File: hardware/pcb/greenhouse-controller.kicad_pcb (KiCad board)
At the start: 2 copper layers, 208 x 132 mm, 68 parts, among them J1 Motor 2, J10 ALARM contact, J11 AC-Mains, J12 DM1AA-SF-PEJ72, J2 24V in, J3 I2C Display, J4 Keypad, J5 MODBUS RS485 S200, J6 Motor 3, J7 Motor 1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

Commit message: Some corrections
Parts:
- added M1: LCD1602 I2C Module mechanical, my-KiCad-library:LCD1602 I2C Module mechanical, F.Cu at (-47.0, 0.00)
- moved P1 2.25 mm to (76.2, 34.0)
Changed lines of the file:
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@@
 		)
 	)
+	(footprint "my-KiCad-library:LCD1602 I2C Module mechanical"
+		(layer "F.Cu")
+		(at -47 0)
+		(property "Reference" "M1"
+			(at 0 -0.5 0)
+			(unlocked yes)
+			(layer "F.SilkS")
+			(effects
+				(font
+					(size 1 1)
+					(thickness 0.1)
+				)
+			)
+		)
+		(property "Value" "LCD1602 I2C Module mechanical"
+			(at 0 1 0)
+			(unlocked yes)
+			(layer "F.Fab")
+			(effects
+				(font
+					(size 1 1)
+					(thickness 0.15)
+				)
+			)
+		)
+		(property "Datasheet" ""
+			(at 0 0 0)
+			(unlocked yes)
+			(layer "F.Fab")
+			(hide yes)
+			(effects
+				(font
+					(size 1 1)
+					(thickness 0.15)
+				)
+			)
+		)
+		(property "Description" ""
+			(at 0 0 0)
+			(unlocked yes)
+			(layer "F.Fab")
+			(hide yes)
+			(effects
+				(font
+					(size 1 1)
+					(thickness 0.15)
+				)
+			)
+		)
+		(sheetname "/")
+		(sheetfile "greenhouse-controller.kicad_sch")
+		(attr through_hole)
+		(fp_rect
+			(start -43.5 -16)
+			(end 43.5 16)
+			(stroke
+				(width 0.1)
+				(type dash)
+			)
+			(fill no)
+			(layer "F.SilkS")
+		)
+		(fp_rect
+			(start -43.5 -7)
+			(end -38 7)
+			(stroke
+				(width 0.1)
+				(type dot)
+			)
+			(fill no)
+			(layer "F.SilkS")
+		)
+		(fp_rect
+			(start -35.65 -13.4)
+			(end 35.65 13.4)
+			(stroke
+				(width 0.05)
+				(type solid)
+			)
+			(fill no)
+			(layer "F.Fab")
+		)
+		(fp_rect
+			(start -32.25 -8)
+			(end 32.25 8)
+			(stroke
+				(width 0.05)
+				(type solid)
+			)
+			(fill no)
+			(layer "F.Fab")
+		)
+		(fp_text user "LCD1602 I2C Module mechanical"
+			(at -20 15 0)
+			(unlocked yes)
+			(layer "F.SilkS")
+			(effects
+				(font
+					(size 1.27 1.27)
+					(thickness 0.15)
+				)
+			)
+		)
+		(fp_text user "${REFERENCE}"
+			(at 0 2.5 0)
+			(unlocked yes)
+			(layer "F.Fab")
+			(effects
+				(font
+					(size 1 1)
+					(thickness 0.15)
+				)
+			)
+		)
+		(pad "" np_thru_hole circle
+			(at -40 -12.5)
+			(size 7 7)
+			(drill 3.2)
+			(layers "*.Cu" "*.Mask")
+		)
+		(pad "" np_thru_hole circle
+			(at -40 12.5)
+			(size 7 7)
+			(drill 3.2)
+			(layers "*.Cu" "*.Mask")
+		)
+		(pad "" np_thru_hole circle
+			(at 40 -12.5)
+			(size 7 7)
+			(drill 3.2)
+			(layers "*.Cu" "*.Mask")
+		)
+		(pad "" np_thru_hole circle
+			(at 40 12.5)
+			(size 7 7)
+			(drill 3.2)
+			(layers "*.Cu" "*.Mask")
+		)
+		(embedded_fonts no)
+	)
 	(footprint "Resistor_SMD:R_1206_3216Metric_Pad1.30x1.75mm_HandSolder"
 		(layer "F.Cu")
@@
 	(footprint "my-KiCad-library:Meanwell RS-15 Mechanical"
 		(layer "F.Cu")
-		(at 77.274 32 90)
+		(at 76.25 34 90)
 		(property "Reference" "P1"
 			(at 31.25 -1.5 90)

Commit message: ìntermediate update of PCB design
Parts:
- moved D14 120.8 mm to (0.00, 32.0)
- moved R22 118.6 mm to (0.00, 36.0), turned to 0 degrees
- moved R24 81.1 mm to (-86.5, 36.0), turned to 0 degrees
- moved D15 77.4 mm to (-89.1, 32.0)
- moved R5 59.3 mm to (-51.5, -27.0), turned to 180 degrees
- moved R16 59.2 mm to (-75.0, -27.0), turned to 180 degrees
- moved R10 59.2 mm to (-28.3, -27.0), turned to 180 degrees
- moved R3 59.1 mm to (-53.1, 28.0), turned to 0 degrees
- moved R14 57.1 mm to (-75.7, 27.0), turned to 0 degrees
- moved R8 57.1 mm to (-30.7, 27.0), turned to 0 degrees
- moved Q5 47.5 mm to (-74.5, 22.0), turned to 180 degrees
- moved Q1 47.4 mm to (-52.0, 22.0), turned to 180 degrees
- moved Q3 47.3 mm to (-29.5, 22.0), turned to 180 degrees
- moved Q2 47.1 mm to (-52.7, -21.0), turned to 0 degrees
- moved Q6 47.1 mm to (-76.3, -21.0), turned to 0 degrees
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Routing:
- net /24V: track 0.00 -> 125.5 mm
- net /24V_GND: track 0.00 -> 112.7 mm
- net /GND: track 0.00 -> 107.8 mm, vias 0 -> 2
- net /SD_CS: track 0.00 -> 101.3 mm
- net Net-(BT1-+): track 0.00 -> 99.2 mm, vias 0 -> 1
- net /SD_MOSI: track 0.00 -> 97.9 mm
- net Net-(J11-Pin_1): track 0.00 -> 93.1 mm
- net Net-(J11-Pin_2): track 0.00 -> 92.1 mm
- net /SD_CLK: track 0.00 -> 91.9 mm
- net Net-(J11-Pin_3): track 0.00 -> 88.3 mm
- net /SD_MISO: track 0.00 -> 85.8 mm
- net /KP_COL1: track 0.00 -> 77.4 mm
- net /KP_ROW4: track 0.00 -> 75.4 mm
- net /KP_ROW3: track 0.00 -> 73.3 mm
- net /KP_ROW2: track 0.00 -> 71.1 mm
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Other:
- board text added: "HB"
- board text added: "PWR"

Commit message: Intermediate update PCB
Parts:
- moved U3 8.28 mm to (6.35, 10.2)
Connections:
- J2 pad 1: /24V_GND -> /GND
- J5 pad 2: /24V_GND -> /GND
- P1 pad 4: /24V_GND -> /GND
- U2 pad 1: Net-(F1-Pad2) -> /24V
- U2 pad 2: Net-(F1-Pad2) -> /24V
- U2 pad 3: /24V_GND -> /GND
- U2 pad 4: /24V_GND -> /GND
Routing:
- net /GND: track 107.8 -> 315.4 mm
- net /HB_LED: track 0.00 -> 153.2 mm, vias 0 -> 1
- net /24V_GND: track 112.7 -> 0.00 mm
- net /24V: track 125.5 -> 221.5 mm
- net /RS485-B: track 12.6 -> 55.4 mm
- net /RS485-A: track 12.5 -> 29.4 mm
- net Net-(F1-Pad2): track 2.54 -> 0.00 mm
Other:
- board text added: "24V"
- board text added: "A"
- board text added: "B"
- board text added: "GND"
- board text added: "RS485"

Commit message: intermediate update PCB
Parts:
- added J8: Load enable, Connector_PinHeader_2.54mm:PinHeader_1x02_P2.54mm_Vertical, F.Cu at (15.0, 26.7)
- moved R21 3.68 mm to (7.34, 26.7)
- moved R3 1.35 mm to (-53.3, 26.7)
- moved R14 0.33 mm to (-75.7, 26.7)
- moved R8 0.33 mm to (-30.7, 26.7)
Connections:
- R21 pad 2: /RS485-B -> Net-(J8-Pin_2)
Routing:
- net /RS485_DI: track 0.00 -> 60.8 mm
- net Net-(J6-Pin_3): track 0.00 -> 58.3 mm
- net Net-(J1-Pin_3): track 0.00 -> 57.6 mm
- net Net-(J7-Pin_3): track 0.00 -> 56.9 mm
- net /RS485_DE_RE: track 0.00 -> 54.1 mm
- net Net-(J6-Pin_4): track 0.00 -> 52.2 mm
- net Net-(J1-Pin_4): track 0.00 -> 51.7 mm
- net Net-(J7-Pin_4): track 0.00 -> 51.2 mm
- net Net-(J1-Pin_2): track 0.00 -> 49.9 mm
- net Net-(J6-Pin_2): track 0.00 -> 49.8 mm
- net Net-(J7-Pin_2): track 0.00 -> 49.2 mm
- net /RS485_RO: track 0.00 -> 48.9 mm
- net Net-(J7-Pin_1): track 0.00 -> 39.8 mm
- net Net-(J1-Pin_1): track 0.00 -> 39.3 mm
- net Net-(J6-Pin_1): track 0.00 -> 38.9 mm
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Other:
- board text added: "CLOSE"
- board text added: "OPEN"

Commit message: First alpha release of PCB
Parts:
- added G***: LOGO_LogoRFSee_28x5-6mm, my-KiCad-library:LOGO_LogoRFSee_28x5-6mm, F.Cu at (181.6, 104.1)
- added G***: LOGO_LogoRFSee_37x8mm, my-KiCad-library:LOGO_LogoRFSee_37x8mm, F.Cu at (83.8, 47.0)
- moved Q3 173.6 mm to (118.5, 112.8)
- moved Q1 173.6 mm to (96.0, 112.8)
- moved Q5 173.6 mm to (73.5, 112.8)
- moved R14 173.6 mm to (72.2, 117.5)
- moved R3 173.6 mm to (94.6, 117.5)
- moved R8 173.6 mm to (117.2, 117.5)
- moved R5 173.5 mm to (96.5, 63.5)
- moved R10 173.4 mm to (119.7, 63.5)
- moved R16 173.4 mm to (73.0, 63.5)
- moved BT1 173.3 mm to (135.0, 31.1)
- moved C2 173.3 mm to (184.2, 54.6)
- moved D10 173.3 mm to (84.0, 122.2)
- moved D13 173.3 mm to (158.1, 125.1)
- moved D14 173.3 mm to (148.0, 122.2)
- moved D15 173.3 mm to (58.9, 122.2)
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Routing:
- net /GND: track 348.2 -> 696.1 mm, vias 5 -> 247
- net /5V: track 68.0 -> 364.8 mm, vias 0 -> 6
- net /OPTO_INPUT: track 8.87 -> 247.2 mm
- net /3V3: track 69.6 -> 190.8 mm, vias 1 -> 4
- net /RELAY_M1_CLOSE: track 0.00 -> 120.2 mm, vias 0 -> 1
- net /RELAY_M1_OPEN: track 0.00 -> 116.9 mm, vias 0 -> 1
- net /RELAY_M2_OPEN: track 5.34 -> 115.0 mm, vias 0 -> 2
- net /RELAY_M3_OPEN: track 5.31 -> 93.3 mm, vias 0 -> 1
- net /RELAY_M3_CLOSE: track 0.00 -> 77.7 mm
- net /RELAY_M2_CLOSE: track 0.00 -> 72.1 mm
- net Net-(D10-K): track 5.90 -> 70.0 mm, vias 0 -> 1
- net Net-(D3-K): track 5.90 -> 69.8 mm, vias 0 -> 1
- net Net-(D6-K): track 5.90 -> 68.9 mm, vias 0 -> 1
- net Net-(D11-A): track 25.2 -> 37.8 mm
- net /SD_MOSI: track 97.9 -> 86.2 mm
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- added copper zone on B.Cu, net /GND
- added copper zone on F.Cu, net /GND
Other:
- outline, holes or cut-outs redrawn
- board text added: "+24V"
- board text added: "220V AC"
- board text added: "ALARM IN"
- board text added: "DICHT"
- board text added: "E"
- board text added: "Enable Load"
- board text added: "K1"
- board text added: "K2"
- board text added: "K3"
- board text added: "K4"
- board text added: "KAS-Controller"
- board text added: "Keypad"
- board text added: "L"
- board text added: "LCD Display"
- board text added: "M1"
- board text added: "M2"
- board text added: "M3"
- board text added: "Motor 1"
- board text added: "Motor 2"
- board text added: "Motor 3"
- board text added: "N"
- board text added: "R1"
- board text added: "R2"
- board text added: "R3"
- board text added: "R4"
- board text added: "RS485 / S200"
- board text added: "RTC Backup"
- board text added: "RUN"
- board text added: "Remko Welling (remko@rfsee.nl) 14-4-2026"
- board text added: "SCL"
- board text added: "SD-Card"
- board text added: "SDA"
- board text added: "VCC"
- board text removed: "HB"

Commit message: Solved final error in PCB, outline Fab text corrected
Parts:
- D14: value LED Amber -> Amber
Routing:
- net /5V: track 364.8 -> 390.6 mm, vias 6 -> 7
- net /GND: vias 247 -> 249
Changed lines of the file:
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@@
 		)
 		(property "Value" "SM712_SOT23"
-			(at 0 2.4 90)
+			(at 4.191 -0.127 180)
 			(layer "F.Fab")
 			(effects
@@
 			)
 		)
-		(property "Value" "LED Amber"
+		(property "Value" "Amber"
 			(at 0 1.65 0)
 			(layer "F.Fab")
@@
 		(tags "capacitor handsolder")
 		(property "Reference" "C3"
-			(at 0 -1.85 0)
+			(at 3.683 0 0)
 			(layer "F.SilkS")
 			(effects
@@
 		)
 		(property "Value" "BUCK-30V-5V"
-			(at 0.0508 -0.127 90)
+			(at 0.0508 -0.127 180)
 			(layer "F.Fab")
 			(effects
@@
 		)
 		(property "Value" "Battery_Cell"
-			(at 12.4 13 270)
+			(at 15.875 -0.173 0)
 			(unlocked yes)
 			(layer "F.Fab")
@@
 		)
 		(fp_text user "${REFERENCE}"
-			(at 12.4 0 270)
+			(at 12.4 0 0)
 			(unlocked yes)
 			(layer "F.Fab")
@@
 		(descr "DS26, Crystal, length 6.0mm, width 2.0mm, THT, https://www.microcrystal.com/fileadmin/Media/Products/32kHz/Datasheet/DS-Series.pdf")
 		(property "Reference" "Y1"
-			(at -1.74 1.625 90)
+			(at 4.043 3.175 180)
 			(layer "F.SilkS")
 			(effects
@@
 		)
 		(property "Value" "32.768 kHz"
-			(at 3.64 1.625 90)
+			(at 0.995 12.065 180)
 			(layer "F.Fab")
 			(effects
@@
 		)
 		(fp_text user "${REFERENCE}"
-			(at 0.95 4.95 90)
+			(at 0.95 10.287 180)
 			(layer "F.Fab")
 			(effects
@@
 		)
 		(property "Value" "I2C Display"
-			(at 0 10 90)
+			(at -0.127 14.097 180)
 			(layer "F.Fab")
 			(effects
@@
 		)
 		(property "Value" "Load enable"
-			(at 0 4.92 90)
+			(at -2.54 4.419 180)
 			(layer "F.Fab")
 			(effects
@@
 		)
 		(property "Value" "1K"
-			(at 0 1.83 0)
+			(at -0.221 -1.846 0)
 			(layer "F.Fab")
 			(effects
@@
 		)
 		(property "Value" "DM1AA-SF-PEJ72"
-			(at 0 1 270)
+			(at 0.690578 0.431176 0)
 			(unlocked yes)
 			(layer "F.Fab")
@@
 		)
 		(fp_text user "${REFERENCE}"
-			(at -0.5 -0.5 270)
+			(at -0.809422 0.931176 0)
 			(unlocked yes)
 			(layer "F.Fab")
@@
 		)
 		(property "Value" "RS-15-24"
-			(at 31.25 0 90)
+			(at 32.045 0.883 0)
 			(unlocked yes)
 			(layer "F.Fab")
@@
 		)
 		(fp_text user "${REFERENCE}"
-			(at 31.25 1.5 90)
+			(at 30.545 0.883 0)
 			(unlocked yes)
 			(layer "F.Fab")
@@
 		)
 		(property "Value" "100n"
-			(at 0 1.85 0)
+			(at 0 -1.905 0)
 			(layer "F.Fab")
 			(effects
@@
 		)
 		(property "Value" "DS1307Z+"
-			(at 0 3.4 90)
+			(at 0.027 7.456 180)
 			(layer "F.Fab")
 			(effects
@@
 	)
 	(via
+		(at 111.506 126.873)
+		(size 0.6)
+		(drill 0.3)
+		(layers "F.Cu" "B.Cu")
+		(free yes)
+		(net 1)
+	)
+	(via
 		(at 168.91 85.09)
 		(size 0.6)
@@
 	)
 	(via
+		(at 111.506 121.412)
+		(size 0.6)
+		(drill 0.3)
+		(layers "F.Cu" "B.Cu")
+		(free yes)
+		(net 1)
+	)
+	(via
 		(at 203.2 50.8)
 		(size 0.6)
@@
 	)
 	(via
-		(at 114.3 127)
+		(at 115.189 126.873)
 		(size 0.6)
 		(drill 0.3)
@@
 	)
 	(via
-		(at 114.3 120.65)
+		(at 115.189 121.412)
 		(size 0.6)
 		(drill 0.3)
@@
 	(segment
 		(start 106.68 128.905)
-		(end 121.285 128.905)
+		(end 114.808 128.905)
 		(width 1)
 		(layer "F.Cu")
@@
 	)
 	(segment
+		(start 114.808 128.905)
+		(end 121.285 128.905)
+		(width 1)
+		(layer "F.Cu")
+		(net 4)
+	)
+	(segment
 		(start 81.105 87.17)
 		(end 83.82 84.455)
@@
 	)
 	(via
+		(at 114.808 128.905)
+		(size 1)
+		(drill 0.5)
+		(layers "F.Cu" "B.Cu")
+		(net 4)
+	)
+	(via
 		(at 145.414999 96.520001)
 		(size 0.8)
@@
 	)
 	(segment
+		(start 114.789372 128.905)
+		(end 114.808 128.905)
+		(width 1)
+		(layer "B.Cu")
+		(net 4)
+	)
+	(segment
 		(start 151.505 76.76)
 		(end 153.255 76.76)
@@
 	)
 	(segment
+		(start 114.475 104.25)
+		(end 114.427 104.298)
+		(width 1)
+		(layer "B.Cu")
+		(net 4)
+	)
+	(segment
 		(start 145.415 96.52)
 		(end 151.765002 96.52)
@@
 	)
 	(segment
+		(start 114.427 107.95)
+		(end 113.299 109.078)
+		(width 1)
+		(layer "B.Cu")
+		(net 4)
+	)
+	(segment
 		(start 189.955 32.93)
 		(end 189.955 30.51)
@@
 	)
 	(segment
+		(start 113.299 127.414628)
+		(end 114.789372 128.905)
+		(width 1)
+		(layer "B.Cu")
+		(net 4)
+	)
+	(segment
 		(start 63.5 128.905)
 		(end 67.945 128.905)
@@
 		(layer "B.Cu")
 		(net 4)
+	)
+	(segment
+		(start 114.427 104.298)
+		(end 114.427 107.95)
+		(width 1)
+		(layer "B.Cu")
+		(net 4)
+	)
+	(segment
+		(start 113.299 109.078)
+		(end 113.299 127.414628)
+		(width 1)
+		(layer "B.Cu")
+		(net 4)

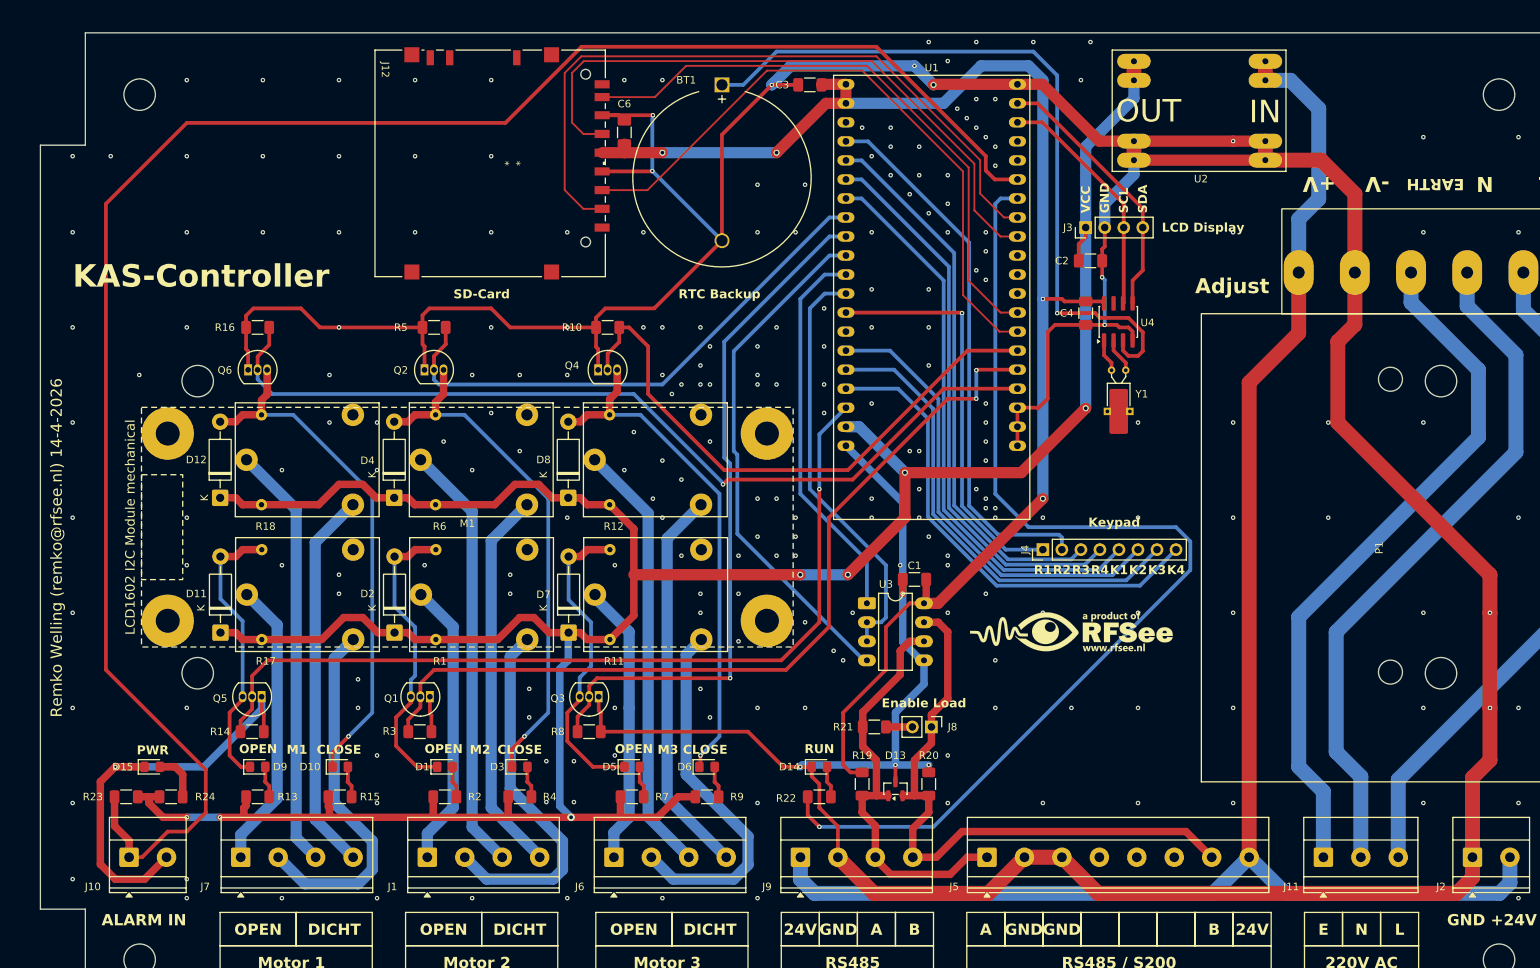
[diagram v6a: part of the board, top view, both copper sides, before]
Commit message: Added RGB-led feature for controller state, added documentation for S200 wind sensor
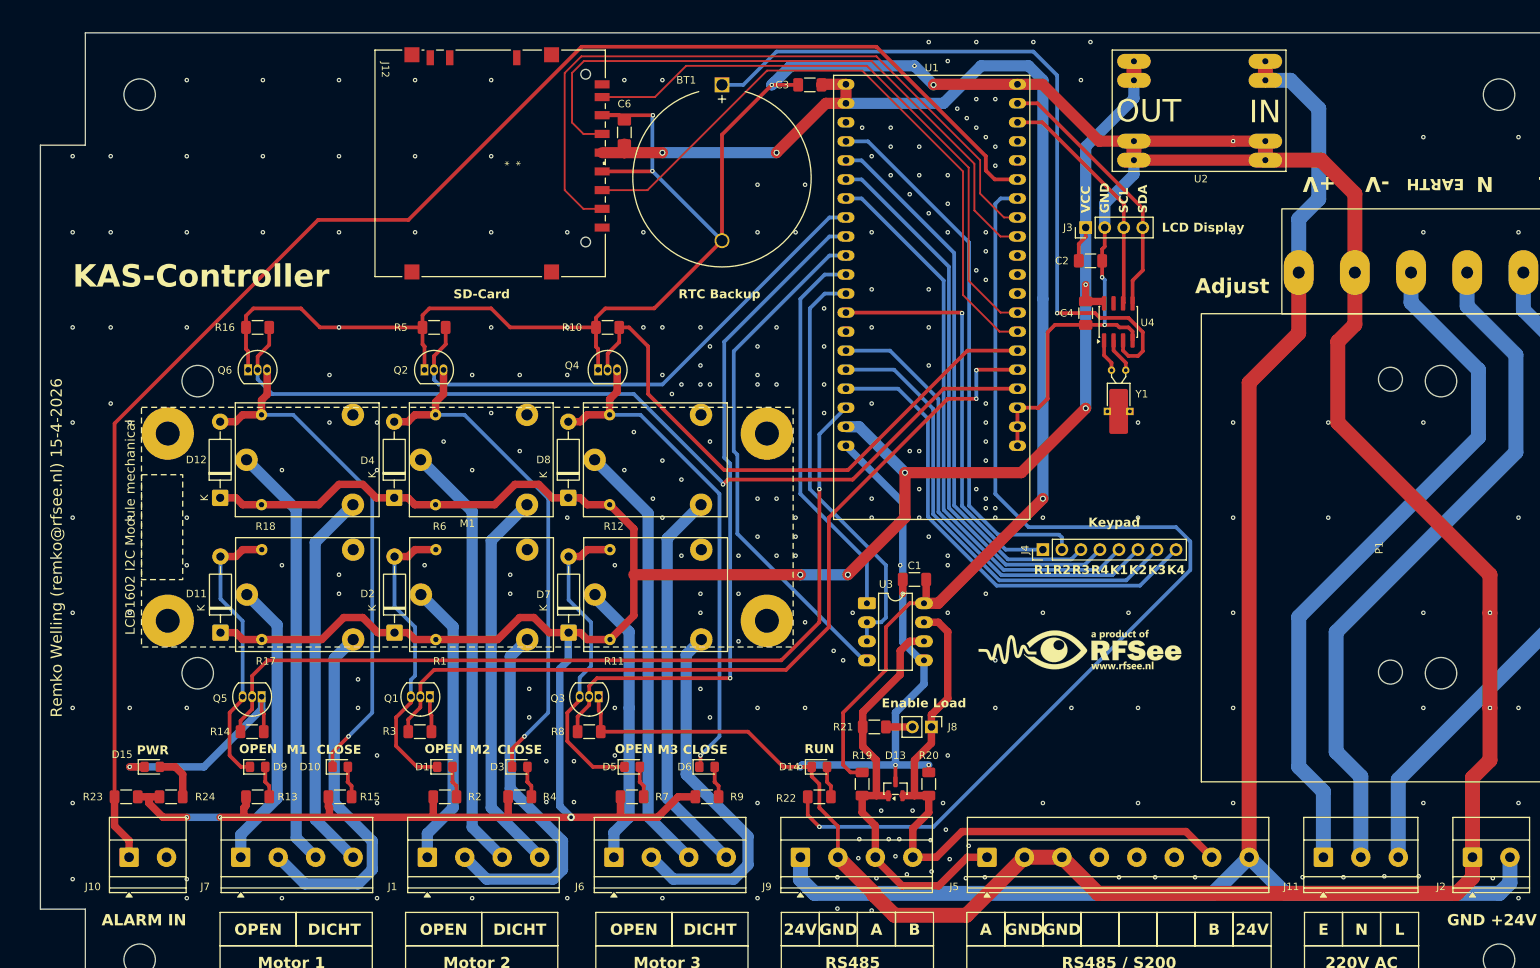
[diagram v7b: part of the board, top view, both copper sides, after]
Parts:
- D14: value Amber -> LED Amber
- moved G*** 2.67 mm to (182.8, 106.6)
- moved G*** 0.97 mm to (84.7, 46.6)
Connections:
- C4 pad 1: /3V3 -> /5V
- U4 pad 8: /3V3 -> /5V
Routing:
- net /OPTO_INPUT: track 247.2 -> 208.6 mm
- net /GND: track 696.1 -> 670.1 mm, vias 249 -> 282
- net /3V3: track 190.8 -> 182.4 mm, vias 4 -> 3
- net /5V: track 390.6 -> 395.4 mm, vias 7 -> 8
- net /RS485-A: track 55.3 -> 56.5 mm
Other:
- board text added: "Remko Welling (remko@rfsee.nl) 15-4-2026"
- board text removed: "Remko Welling (remko@rfsee.nl) 14-4-2026"
